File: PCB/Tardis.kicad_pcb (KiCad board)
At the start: 4 copper layers, 99.1 x 152.4 mm, 141 parts, among them J1 CONN_01X01, J10 CONN_01X01, J11 CONN_01X01, J12 CONN_01X01, J13 CONN_01X01, J14 CONN_01X01, J15 CONN_01X01, J16 CONN_01X01, J2 CONN_01X01, J3 CONN_01X01, J4 CONN_01X01, J5 CONN_01X01, J6 CONN_01X01, J7 CONN_01X01, J8 CONN_01X01, J9 CONN_01X01, Q1 2N3904, Q2 2N3904, Q3 2N3904, Q4 2N3904, Q5 2N3904, Q6 2N3904, Q7 2N3904, U1 L4940, U2 MT8888C, U3 MT8888C, U4 ATMEGA328P-AU, U5 ATMEGA328P-AU, U6 ATMEGA328P-AU, U7 LM324N, U8 TS4990IST, U9 TS4990IST, Y1 3.579545MHz, Y2 3.579545MHz, Y3 Crystal_GND2, Y4 Crystal_GND2, Y5 Crystal_GND2

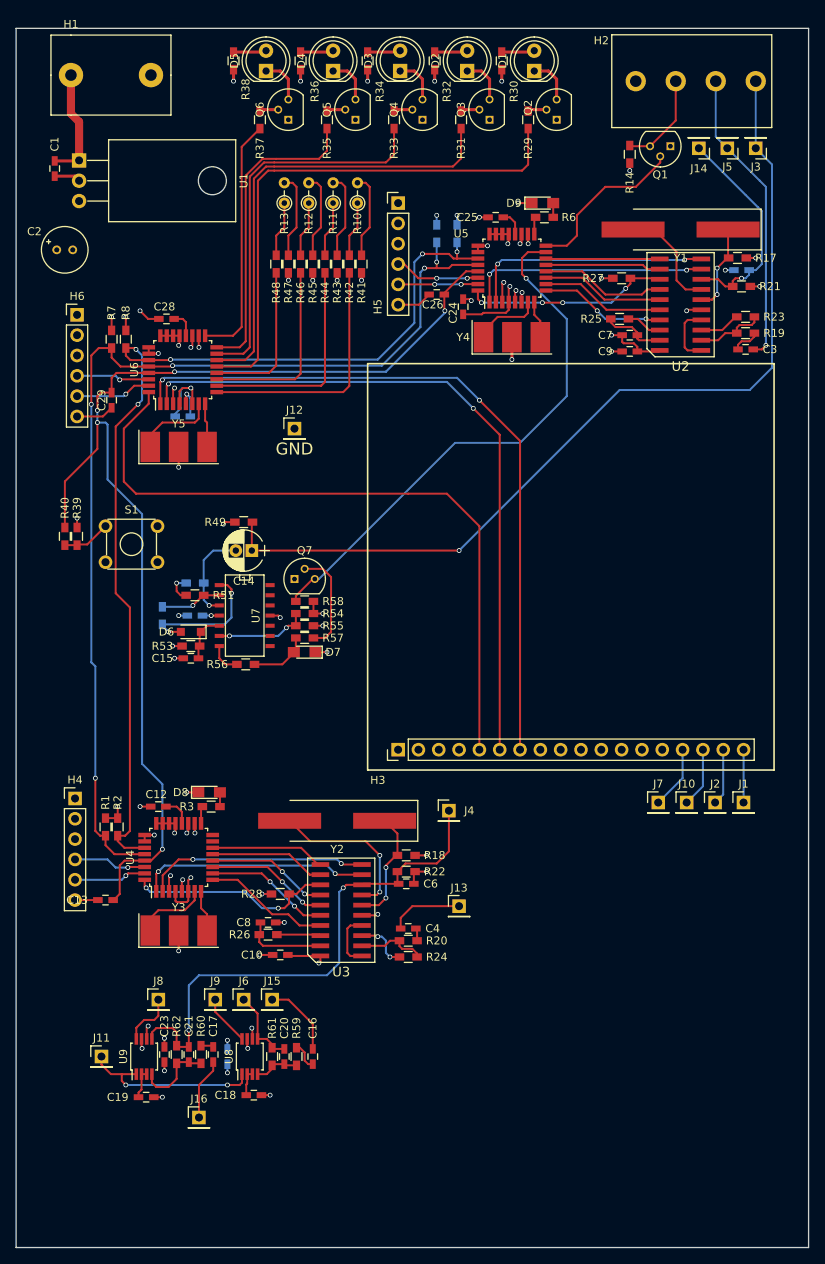
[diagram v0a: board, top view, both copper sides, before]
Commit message: Removed Raycast, implemented spawning bullets.
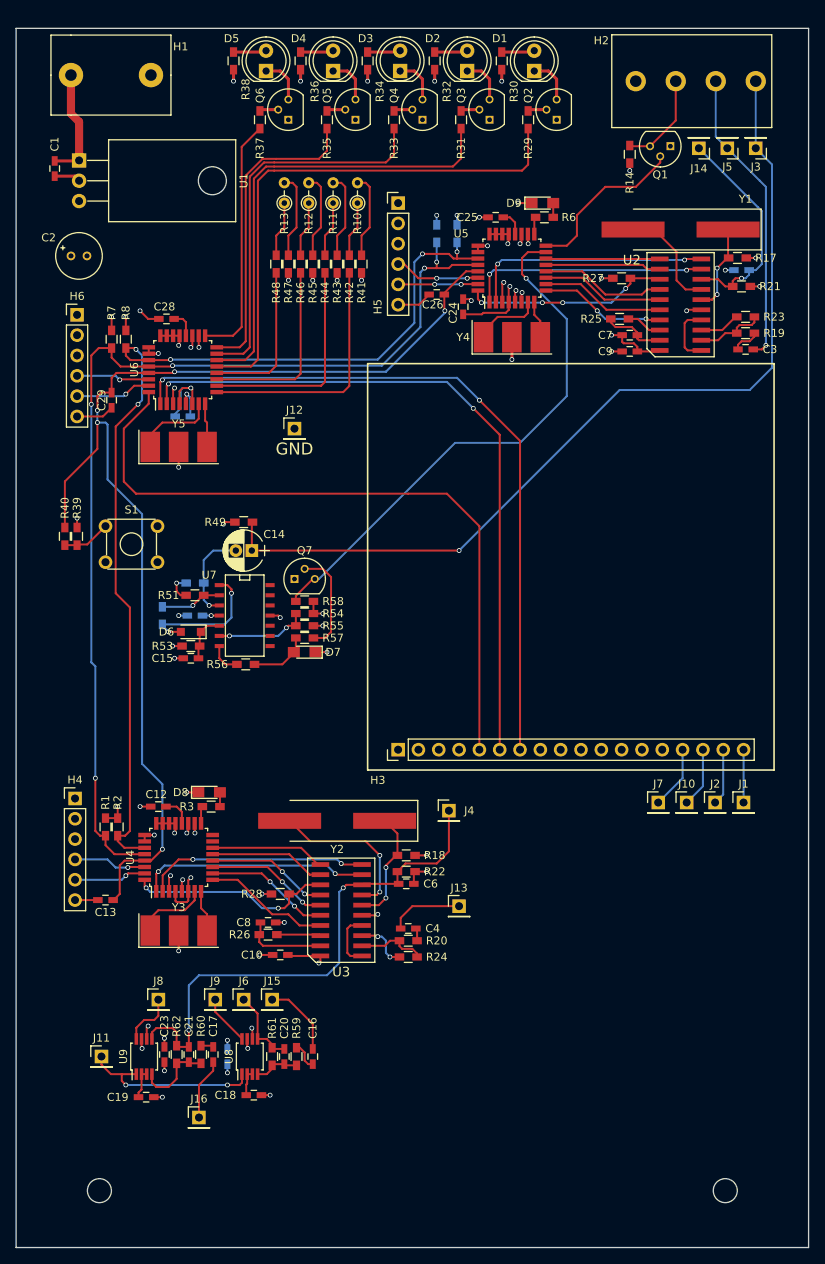
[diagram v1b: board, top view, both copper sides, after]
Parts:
- added REF**: MountingHole_3mm, Mounting_Holes:MountingHole_3mm, F.Cu at (188.2, 158.0)
- added REF**: MountingHole_3mm, Mounting_Holes:MountingHole_3mm, F.Cu at (266.4, 158.0)
- moved C2 1.93 mm to (184.7, 41.1)
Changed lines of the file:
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@@
     (links 312)
     (no_connects 8)
-    (area 177.787299 11.217 276.872701 165.112701)
+    (area 177.787299 12.687299 276.872701 165.112701)
     (thickness 1.6)
     (drawings 20)
     (tracks 1012)
     (zones 0)
-    (modules 141)
+    (modules 143)
     (nets 140)
   )
@@
   (layers
     (0 F.Cu signal)
-    (1 In1.Cu power)
-    (2 In2.Cu power)
+    (1 In1.Cu power hide)
+    (2 In2.Cu power hide)
     (31 B.Cu signal)
     (32 B.Adhes user)
@@
     (visible_elements 7FFFFFFF)
     (pcbplotparams
-      (layerselection 0x311fc_80000007)
+      (layerselection 0x000c0_00000000)
       (usegerberextensions false)
       (excludeedgelayer true)
@@
       (effects (font (size 1 1) (thickness 0.15)))
     )
-    (fp_text value 1935187 (at 1.016 7.112 180) (layer F.Fab)
+    (fp_text value 1935187 (at 7.112 4.572 180) (layer F.Fab)
       (effects (font (size 1 1) (thickness 0.15)))
     )
@@
     (descr "TO-92 leads molded, narrow, drill 0.6mm (see NXP sot054_po.pdf)")
     (tags "to-92 sc-43 sc-43a sot54 PA33 transistor")
-    (fp_text reference Q2 (at 1.524 -3.556 90) (layer F.SilkS)
+    (fp_text reference Q2 (at 3.048 -3.556 90) (layer F.SilkS)
       (effects (font (size 1 1) (thickness 0.15)))
     )
@@
   )
   (module Footprints:RADIAL_5MM (layer F.Cu)
-    (at 182.88 40.386)
+    (at 184.658 41.148)
     (fp_text reference C2 (at -2.794 -2.286 180) (layer F.SilkS)
       (effects (font (size 1 1) (thickness 0.15)))
@@
     (descr "TO-92 leads molded, narrow, drill 0.6mm (see NXP sot054_po.pdf)")
     (tags "to-92 sc-43 sc-43a sot54 PA33 transistor")
-    (fp_text reference Q3 (at 1.27 -3.56 90) (layer F.SilkS)
+    (fp_text reference Q3 (at 3.048 -3.556 90) (layer F.SilkS)
       (effects (font (size 1 1) (thickness 0.15)))
     )
@@
     (descr "TO-92 leads molded, narrow, drill 0.6mm (see NXP sot054_po.pdf)")
     (tags "to-92 sc-43 sc-43a sot54 PA33 transistor")
-    (fp_text reference Q4 (at 1.27 -3.56 90) (layer F.SilkS)
+    (fp_text reference Q4 (at 3.048 -3.556 90) (layer F.SilkS)
       (effects (font (size 1 1) (thickness 0.15)))
     )
@@
     (descr "TO-92 leads molded, narrow, drill 0.6mm (see NXP sot054_po.pdf)")
     (tags "to-92 sc-43 sc-43a sot54 PA33 transistor")
-    (fp_text reference Q5 (at 1.27 -3.56 90) (layer F.SilkS)
+    (fp_text reference Q5 (at 3.048 -3.556 90) (layer F.SilkS)
       (effects (font (size 1 1) (thickness 0.15)))
     )
@@
     (descr "TO-92 leads molded, narrow, drill 0.6mm (see NXP sot054_po.pdf)")
     (tags "to-92 sc-43 sc-43a sot54 PA33 transistor")
-    (fp_text reference Q6 (at 1.27 -3.56 90) (layer F.SilkS)
+    (fp_text reference Q6 (at 3.048 -3.556 90) (layer F.SilkS)
       (effects (font (size 1 1) (thickness 0.15)))
     )
@@
     (tags "capacitor 0603")
     (attr smd)
-    (fp_text reference C13 (at -3.556 0) (layer F.SilkS)
+    (fp_text reference C13 (at 0 1.524) (layer F.SilkS)
       (effects (font (size 1 1) (thickness 0.15)))
     )
@@
     (descr "CP, Radial series, Radial, pin pitch=2.00mm, , diameter=5mm, Electrolytic Capacitor")
     (tags "CP Radial series Radial pin pitch 2.00mm  diameter 5mm Electrolytic Capacitor")
-    (fp_text reference C14 (at 1 -3.81 180) (layer F.SilkS)
+    (fp_text reference C14 (at -2.794 2.032 180) (layer F.SilkS)
       (effects (font (size 1 1) (thickness 0.15)))
     )
@@
   (module Footprints:ED800 (layer F.Cu)
     (at 184.658 18.542)
-    (fp_text reference H1 (at 0 -6.35) (layer F.SilkS)
+    (fp_text reference H1 (at 13.716 -3.556) (layer F.SilkS)
       (effects (font (size 1 1) (thickness 0.15)))
     )
@@
       (effects (font (size 1 1) (thickness 0.15)))
     )
-    (fp_text value 1k (at 0 0 270) (layer F.Fab)
+    (fp_text value 1k (at 0.254 0 270) (layer F.Fab)
       (effects (font (size 1 1) (thickness 0.15)))
     )
@@
     (tags "resistor 0603")
     (attr smd)
-    (fp_text reference R51 (at -3.556 0 180) (layer F.SilkS)
+    (fp_text reference R51 (at 3.302 0 180) (layer F.SilkS)
       (effects (font (size 1 1) (thickness 0.15)))
     )
@@
   (module Footprints:SOIC-20 (layer F.Cu)
     (at 260.858 47.244 90)
-    (fp_text reference U2 (at -7.715 0 180) (layer F.SilkS)
+    (fp_text reference U2 (at 5.588 -6.096 180) (layer F.SilkS)
       (effects (font (size 1.2 1.2) (thickness 0.15)))
     )
@@
     (tags "CMS SOJ")
     (attr smd)
-    (fp_text reference U7 (at 0 -1.27 270) (layer F.SilkS)
+    (fp_text reference U7 (at -5.08 4.572 360) (layer F.SilkS)
       (effects (font (size 1 1) (thickness 0.15)))
     )
@@
     (descr "LED, diameter 5.0mm, 2 pins, http://cdn-reichelt.de/documents/datenblatt/A500/LL-504BC2E-009.pdf")
     (tags "LED diameter 5.0mm 2 pins")
-    (fp_text reference D1 (at 1.27 -3.96 90) (layer F.SilkS)
+    (fp_text reference D1 (at 4.064 -4.318 180) (layer F.SilkS)
       (effects (font (size 1 1) (thickness 0.15)))
     )
@@
     (descr "LED, diameter 5.0mm, 2 pins, http://cdn-reichelt.de/documents/datenblatt/A500/LL-504BC2E-009.pdf")
     (tags "LED diameter 5.0mm 2 pins")
-    (fp_text reference D2 (at 1.27 -3.96 90) (layer F.SilkS)
+    (fp_text reference D2 (at 4.064 -4.318 180) (layer F.SilkS)
       (effects (font (size 1 1) (thickness 0.15)))
     )
@@
     (descr "LED, diameter 5.0mm, 2 pins, http://cdn-reichelt.de/documents/datenblatt/A500/LL-504BC2E-009.pdf")
     (tags "LED diameter 5.0mm 2 pins")
-    (fp_text reference D3 (at 1.27 -3.96 90) (layer F.SilkS)
+    (fp_text reference D3 (at 4.064 -4.318 180) (layer F.SilkS)
       (effects (font (size 1 1) (thickness 0.15)))
     )
@@
     (descr "LED, diameter 5.0mm, 2 pins, http://cdn-reichelt.de/documents/datenblatt/A500/LL-504BC2E-009.pdf")
     (tags "LED diameter 5.0mm 2 pins")
-    (fp_text reference D4 (at 1.27 -3.96 90) (layer F.SilkS)
+    (fp_text reference D4 (at 4.064 -4.318 180) (layer F.SilkS)
       (effects (font (size 1 1) (thickness 0.15)))
     )
@@
     (descr "LED, diameter 5.0mm, 2 pins, http://cdn-reichelt.de/documents/datenblatt/A500/LL-504BC2E-009.pdf")
     (tags "LED diameter 5.0mm 2 pins")
-    (fp_text reference D5 (at 1.27 -3.96 90) (layer F.SilkS)
+    (fp_text reference D5 (at 4.064 -4.318 180) (layer F.SilkS)
       (effects (font (size 1 1) (thickness 0.15)))
     )
@@
     (tags "SMD SMT crystal hand-soldering")
     (attr smd)
-    (fp_text reference Y1 (at 0 -3.55 180) (layer F.SilkS)
+    (fp_text reference Y1 (at -8.128 3.81 180) (layer F.SilkS)
       (effects (font (size 1 1) (thickness 0.15)))
     )
@@
     )
   )
+  (module Mounting_Holes:MountingHole_3mm (layer F.Cu)
+    (at 188.214 157.988)
+    (descr "Mounting Hole 3mm, no annular")
+    (tags "mounting hole 3mm no annular")
+    (attr virtual)
+    (fp_text reference REF** (at 0 -4) (layer F.SilkS) hide
+      (effects (font (size 1 1) (thickness 0.15)))
+    )
+    (fp_text value MountingHole_3mm (at 0 4) (layer F.Fab)
+      (effects (font (size 1 1) (thickness 0.15)))
+    )
+    (fp_text user %R (at 0.3 0) (layer F.Fab)
+      (effects (font (size 1 1) (thickness 0.15)))
+    )
+    (fp_circle (center 0 0) (end 3 0) (layer Cmts.User) (width 0.15))
+    (fp_circle (center 0 0) (end 3.25 0) (layer F.CrtYd) (width 0.05))
+    (pad 1 np_thru_hole circle (at 0 0) (size 3 3) (drill 3) (layers *.Cu *.Mask))
+  )
+  (module Mounting_Holes:MountingHole_3mm (layer F.Cu)
+    (at 266.446 157.988)
+    (descr "Mounting Hole 3mm, no annular")
+    (tags "mounting hole 3mm no annular")
+    (attr virtual)
+    (fp_text reference REF** (at 0 -4) (layer F.SilkS) hide
+      (effects (font (size 1 1) (thickness 0.15)))
+    )
+    (fp_text value MountingHole_3mm (at 0 4) (layer F.Fab)
+      (effects (font (size 1 1) (thickness 0.15)))
+    )
+    (fp_text user %R (at 0.3 0) (layer F.Fab)
+      (effects (font (size 1 1) (thickness 0.15)))
+    )
+    (fp_circle (center 0 0) (end 3 0) (layer Cmts.User) (width 0.15))
+    (fp_circle (center 0 0) (end 3.25 0) (layer F.CrtYd) (width 0.05))
+    (pad 1 np_thru_hole circle (at 0 0) (size 3 3) (drill 3) (layers *.Cu *.Mask))
+  )
   (gr_line (start 178.308 16.764) (end 178.308 13.208) (angle 90) (layer Margin) (width 0.2))
